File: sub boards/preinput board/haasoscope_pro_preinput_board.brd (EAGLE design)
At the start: 94.2 x 72.7 mm, 55 parts, among them J4 8pin, K1 G6K-2F-RF-T-TR03_DC5, K2 G6K-2F-RF-T-TR03_DC5, K3 TLP3475R_TP,F, K5 G6K-2F-RF-T-TR03_DC5, Q1 S8050, Q2 S8050, Q3 S8050

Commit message: update filter component values
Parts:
- C4: value 2pF -> 1.2pF
- C5: value 3pF -> 1.5pF
- C6: value 3pF -> 1.0pF
- C7: value 4.3pF -> 2.4pF
- C8: value 6.2pF -> 3.3pF
- C9: value 6.2pF -> 2.4pF
- L2: value 3.9nH -> 5.1nH
- L3: value 2.7nH -> 3.9nH
- L4: value 8.2nH -> 7.5nH
- L5: value 8.2nH -> 10nH
- L6: value 5.6nH -> 7.5nH
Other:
- board text added: "1.0pF"
- board text added: "1.2pF"
- board text added: "1.5pF"
- board text added: "2.4pF"
- board text added: "3.3pF"
- board text removed: "2pF"
- board text removed: "3pF"
- board text removed: "4.3pF"
- board text removed: "6.2pF"

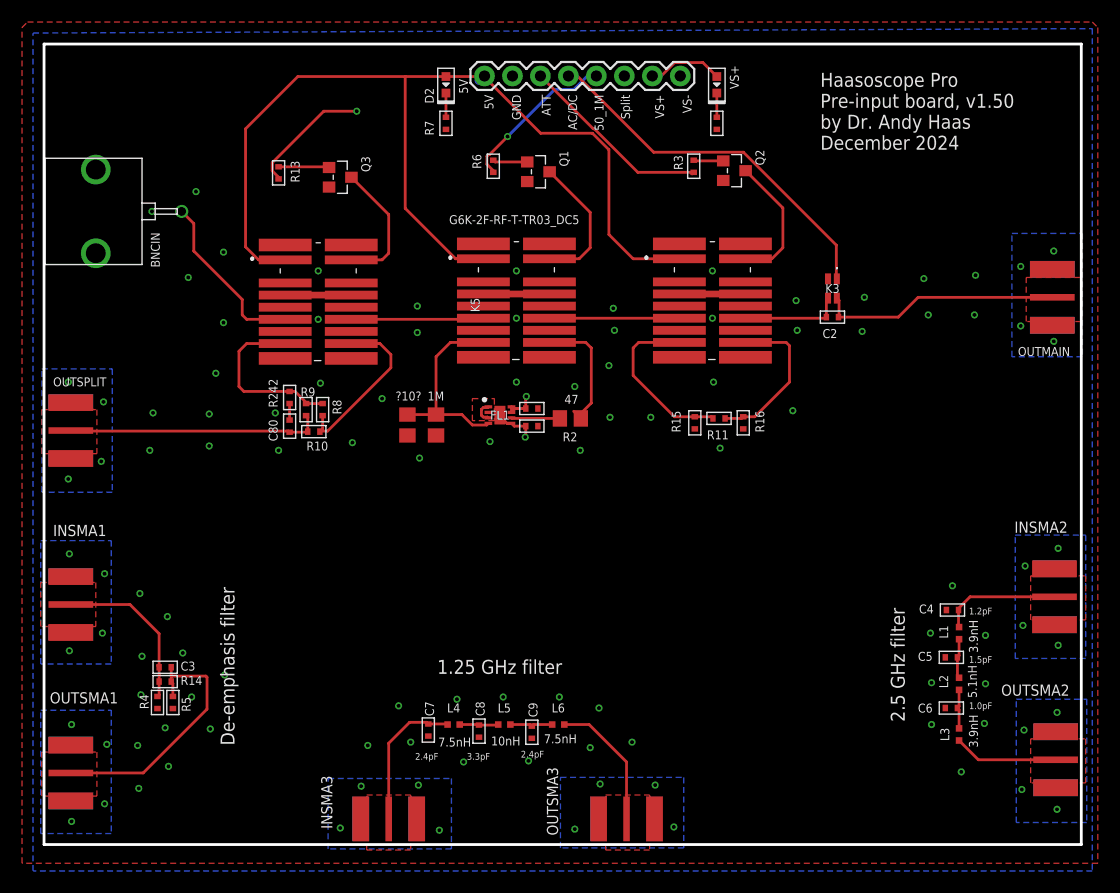
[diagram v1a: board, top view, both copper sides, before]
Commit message: update filter values, 5th order
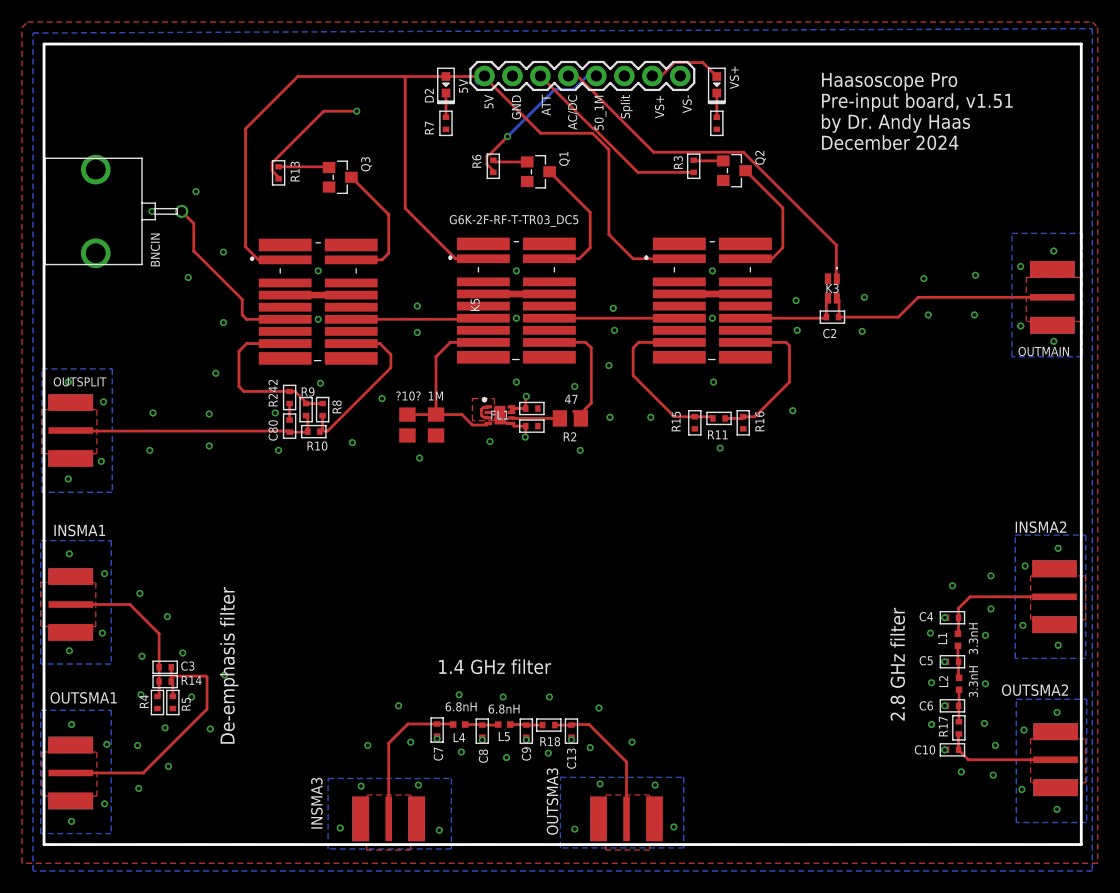
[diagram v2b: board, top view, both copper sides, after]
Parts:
- removed L3: 3.9nH, Nordic_nRF:RESC0402_N
- removed L6: 7.5nH, Nordic_nRF:RESC0402_N
- added C10, C13: ?0pF?, MF_Passives:C0402
- added R17, R18: 0, MF_Passives:R0402
- C4: value 1.2pF -> 1.0pF
- C7, C9: value 2.4pF -> 3.0pF
- C8: value 3.3pF -> 4.3pF
- L1: value 3.9nH -> 3.3nH
- L2: value 5.1nH -> 3.3nH
- L4: value 7.5nH -> 6.8nH
- L5: value 10nH -> 6.8nH
- moved C7 0.80 mm to (26.5, -12.3)
- moved C4 0.70 mm to (73.3, -2.10)
- moved L1 0.61 mm to (73.8, -4.10)
- moved C9 0.51 mm to (34.6, -12.4)
- moved L4 0.50 mm to (28.5, -11.8)
- moved C5 0.41 mm to (73.3, -6.10)
- moved C8 0.30 mm to (30.6, -12.4)
- moved C6 0.22 mm to (73.3, -10.1)
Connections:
- net GND: now also C10.P$2, C13.P$2
- net N$11: now also R18.P$2; no longer L6.1
- net N$9: now also R17.P$2; no longer L3.1
- net SMAOUT2: now also C10.P$1, R17.P$1; no longer L3.2
- net SMAOUT3: now also C13.P$1, R18.P$1; no longer L6.2
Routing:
- net SMAOUT2: track 9.49 -> 12.1 mm
- net N$11: track 3.92 -> 3.03 mm
- net SMAOUT3: track 12.2 -> 13.1 mm
- net N$8: track 3.62 -> 2.94 mm
- net SMAIN2: track 10.9 -> 11.5 mm
- net N$10: track 3.54 -> 3.04 mm
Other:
- board text added: "1.4 GHz filter"
- board text added: "2.8 GHz filter"
- board text added: "Haasoscope Pro Pre-input board, v1.51 by Dr. Andy Haas December 2024"
- board text removed: "1.0pF"
- board text removed: "1.25 GHz filter"
- board text removed: "1.2pF"
- board text removed: "1.5pF"
- board text removed: "2.4pF"
- board text removed: "2.5 GHz filter"
- board text removed: "3.3pF"
- board text removed: "Haasoscope Pro Pre-input board, v1.50 by Dr. Andy Haas December 2024"
